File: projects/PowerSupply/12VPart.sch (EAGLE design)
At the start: 26 parts, among them IC1 LM2596T, IC2 LM2596T, X1 IN, X2 OUT

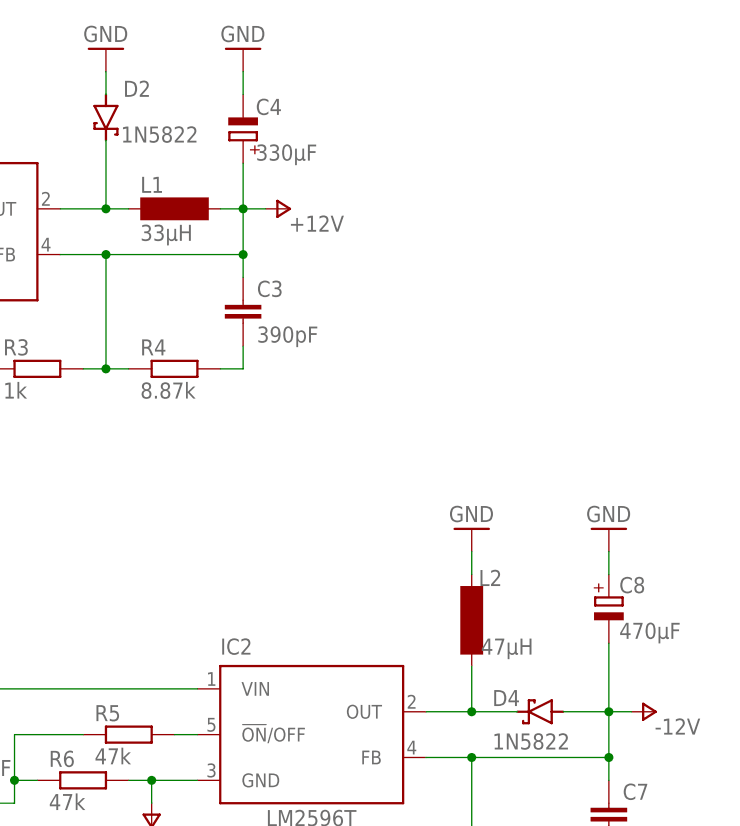
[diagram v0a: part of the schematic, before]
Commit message: feat: 12 volt part modified
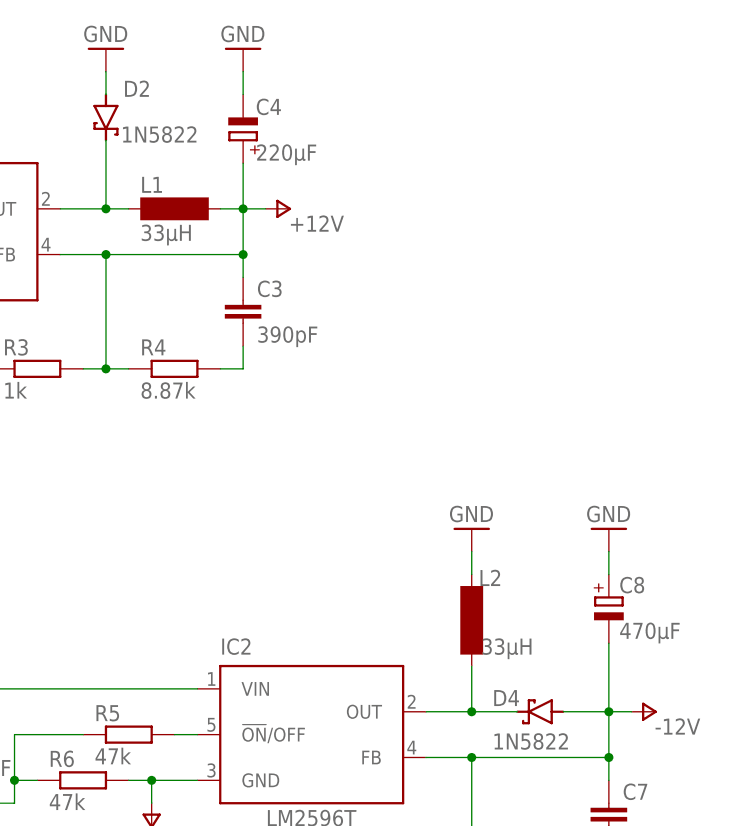
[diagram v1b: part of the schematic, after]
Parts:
- C4: value 330µF -> 220µF
- L1: device inductor-neosid:SD12-680 -> bb84:IND-120-330K
- L2: value 47µH -> 33µH; device inductor-neosid:SD12-680 -> bb84:IND-120-330K
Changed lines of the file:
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@@
 <grid distance="0.1" unitdist="inch" unit="inch" style="lines" multiple="1" display="no" altdistance="0.01" altunitdist="inch" altunit="inch"/>
 <layers>
-<layer number="1" name="Top" color="4" fill="1" visible="no" active="no"/>
-<layer number="16" name="Bottom" color="1" fill="1" visible="no" active="no"/>
-<layer number="17" name="Pads" color="2" fill="1" visible="no" active="no"/>
-<layer number="18" name="Vias" color="2" fill="1" visible="no" active="no"/>
-<layer number="19" name="Unrouted" color="6" fill="1" visible="no" active="no"/>
-<layer number="20" name="Dimension" color="24" fill="1" visible="no" active="no"/>
-<layer number="21" name="tPlace" color="7" fill="1" visible="no" active="no"/>
-<layer number="22" name="bPlace" color="7" fill="1" visible="no" active="no"/>
-<layer number="23" name="tOrigins" color="15" fill="1" visible="no" active="no"/>
-<layer number="24" name="bOrigins" color="15" fill="1" visible="no" active="no"/>
-<layer number="25" name="tNames" color="7" fill="1" visible="no" active="no"/>
-<layer number="26" name="bNames" color="7" fill="1" visible="no" active="no"/>
-<layer number="27" name="tValues" color="7" fill="1" visible="no" active="no"/>
-<layer number="28" name="bValues" color="7" fill="1" visible="no" active="no"/>
+<layer number="1" name="Top" color="4" fill="1" visible="yes" active="no"/>
+<layer number="16" name="Bottom" color="1" fill="1" visible="yes" active="no"/>
+<layer number="17" name="Pads" color="2" fill="1" visible="yes" active="no"/>
+<layer number="18" name="Vias" color="2" fill="1" visible="yes" active="no"/>
+<layer number="19" name="Unrouted" color="6" fill="1" visible="yes" active="no"/>
+<layer number="20" name="Dimension" color="24" fill="1" visible="yes" active="no"/>
+<layer number="21" name="tPlace" color="7" fill="1" visible="yes" active="no"/>
+<layer number="22" name="bPlace" color="7" fill="1" visible="yes" active="no"/>
+<layer number="23" name="tOrigins" color="15" fill="1" visible="yes" active="no"/>
+<layer number="24" name="bOrigins" color="15" fill="1" visible="yes" active="no"/>
+<layer number="25" name="tNames" color="7" fill="1" visible="yes" active="no"/>
+<layer number="26" name="bNames" color="7" fill="1" visible="yes" active="no"/>
+<layer number="27" name="tValues" color="7" fill="1" visible="yes" active="no"/>
+<layer number="28" name="bValues" color="7" fill="1" visible="yes" active="no"/>
 <layer number="29" name="tStop" color="7" fill="3" visible="no" active="no"/>
 <layer number="30" name="bStop" color="7" fill="6" visible="no" active="no"/>
@@
 <layer number="35" name="tGlue" color="7" fill="4" visible="no" active="no"/>
 <layer number="36" name="bGlue" color="7" fill="5" visible="no" active="no"/>
-<layer number="37" name="tTest" color="7" fill="1" visible="no" active="no"/>
-<layer number="38" name="bTest" color="7" fill="1" visible="no" active="no"/>
+<layer number="37" name="tTest" color="7" fill="1" visible="yes" active="no"/>
+<layer number="38" name="bTest" color="7" fill="1" visible="yes" active="no"/>
 <layer number="39" name="tKeepout" color="4" fill="11" visible="no" active="no"/>
 <layer number="40" name="bKeepout" color="1" fill="11" visible="no" active="no"/>
@@
 <layer number="44" name="Drills" color="7" fill="1" visible="no" active="no"/>
 <layer number="45" name="Holes" color="7" fill="1" visible="no" active="no"/>
-<layer number="46" name="Milling" color="3" fill="1" visible="no" active="no"/>
-<layer number="47" name="Measures" color="7" fill="1" visible="no" active="no"/>
-<layer number="48" name="Document" color="7" fill="1" visible="no" active="no"/>
-<layer number="49" name="Reference" color="7" fill="1" visible="no" active="no"/>
-<layer number="51" name="tDocu" color="7" fill="1" visible="no" active="no"/>
-<layer number="52" name="bDocu" color="7" fill="1" visible="no" active="no"/>
+<layer number="46" name="Milling" color="3" fill="1" visible="yes" active="no"/>
+<layer number="47" name="Measures" color="7" fill="1" visible="yes" active="no"/>
+<layer number="48" name="Document" color="7" fill="1" visible="yes" active="no"/>
+<layer number="49" name="Reference" color="7" fill="1" visible="yes" active="no"/>
+<layer number="51" name="tDocu" color="7" fill="1" visible="yes" active="no"/>
+<layer number="52" name="bDocu" color="7" fill="1" visible="yes" active="no"/>
 <layer number="88" name="SimResults" color="9" fill="1" visible="yes" active="yes"/>
 <layer number="89" name="SimProbes" color="9" fill="1" visible="yes" active="yes"/>
@@
 <part name="D2" library="diode" library_urn="urn:adsk.eagle:library:210" deviceset="SCHOTTKY-DIODE" device="C4111-15" package3d_urn="urn:adsk.eagle:package:43355/2" value="1N5822"/>
 <part name="GND5" library="supply1" library_urn="urn:adsk.eagle:library:371" deviceset="GND" device=""/>
-<part name="L1" library="inductor-neosid" library_urn="urn:adsk.eagle:library:241" deviceset="SD12" device="-680" package3d_urn="urn:adsk.eagle:package:14657/1" value="33µH"/>
-<part name="C4" library="rcl" library_urn="urn:adsk.eagle:library:334" deviceset="CPOL-EU" device="E3.5-8" package3d_urn="urn:adsk.eagle:package:23360/2" value="330µF"/>
+<part name="L1" library="bb84" deviceset="IND-120-330K" device="" value="33µH"/>
+<part name="C4" library="rcl" library_urn="urn:adsk.eagle:library:334" deviceset="CPOL-EU" device="E3.5-8" package3d_urn="urn:adsk.eagle:package:23360/2" value="220µF"/>
 <part name="X2" library="con-wago-508" library_urn="urn:adsk.eagle:library:196" deviceset="W237-03P" device="" package3d_urn="urn:adsk.eagle:package:10737/1" value="OUT"/>
 <part name="GND7" library="supply1" library_urn="urn:adsk.eagle:library:371" deviceset="GND" device=""/>
 <part name="IC2" library="national-semiconductor" library_urn="urn:adsk.eagle:library:307" deviceset="LM2596" device="T" package3d_urn="urn:adsk.eagle:package:21216/1"/>
-<part name="L2" library="inductor-neosid" library_urn="urn:adsk.eagle:library:241" deviceset="SD12" device="-680" package3d_urn="urn:adsk.eagle:package:14657/1" value="47µH"/>
+<part name="L2" library="bb84" deviceset="IND-120-330K" device="" value="33µH"/>
 <part name="GND9" library="supply1" library_urn="urn:adsk.eagle:library:371" deviceset="GND" device=""/>
 <part name="D4" library="diode" library_urn="urn:adsk.eagle:library:210" deviceset="SCHOTTKY-DIODE" device="C4111-15" package3d_urn="urn:adsk.eagle:package:43355/2" value="1N5822"/>

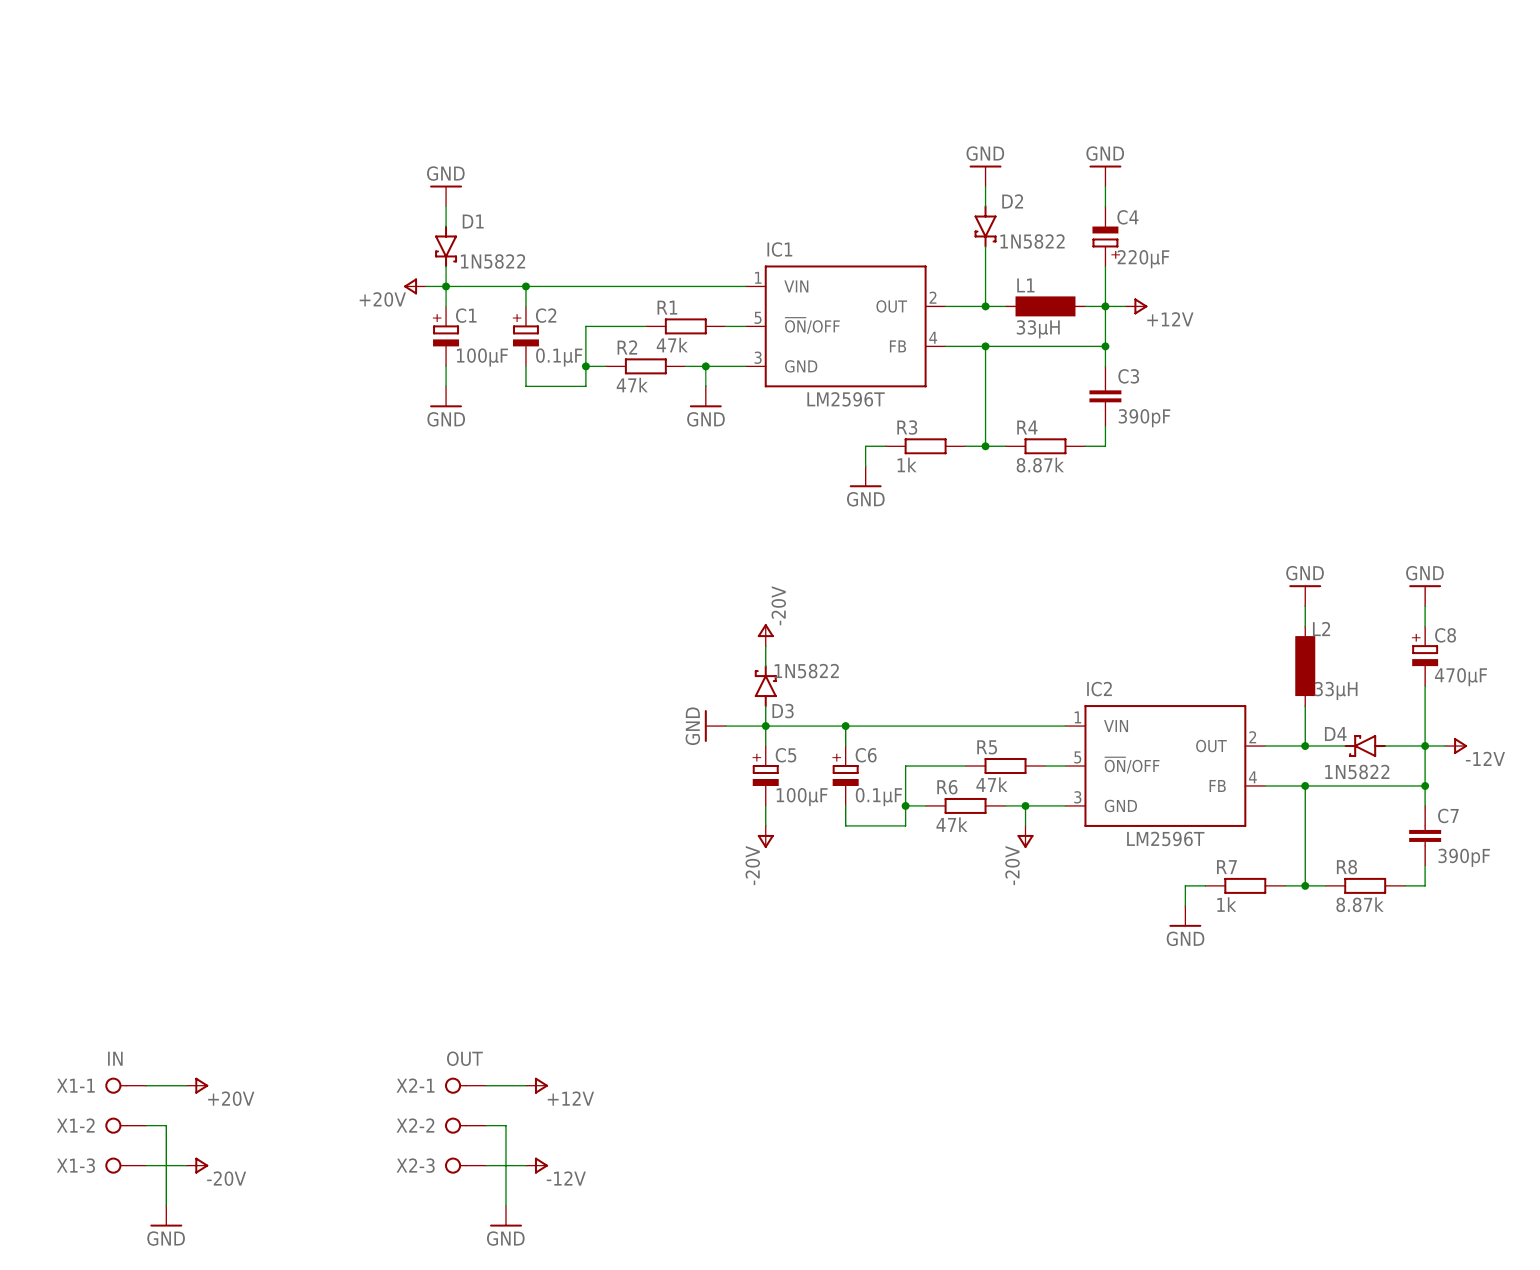
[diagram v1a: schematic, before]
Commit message: feat: modified 12 volt parts
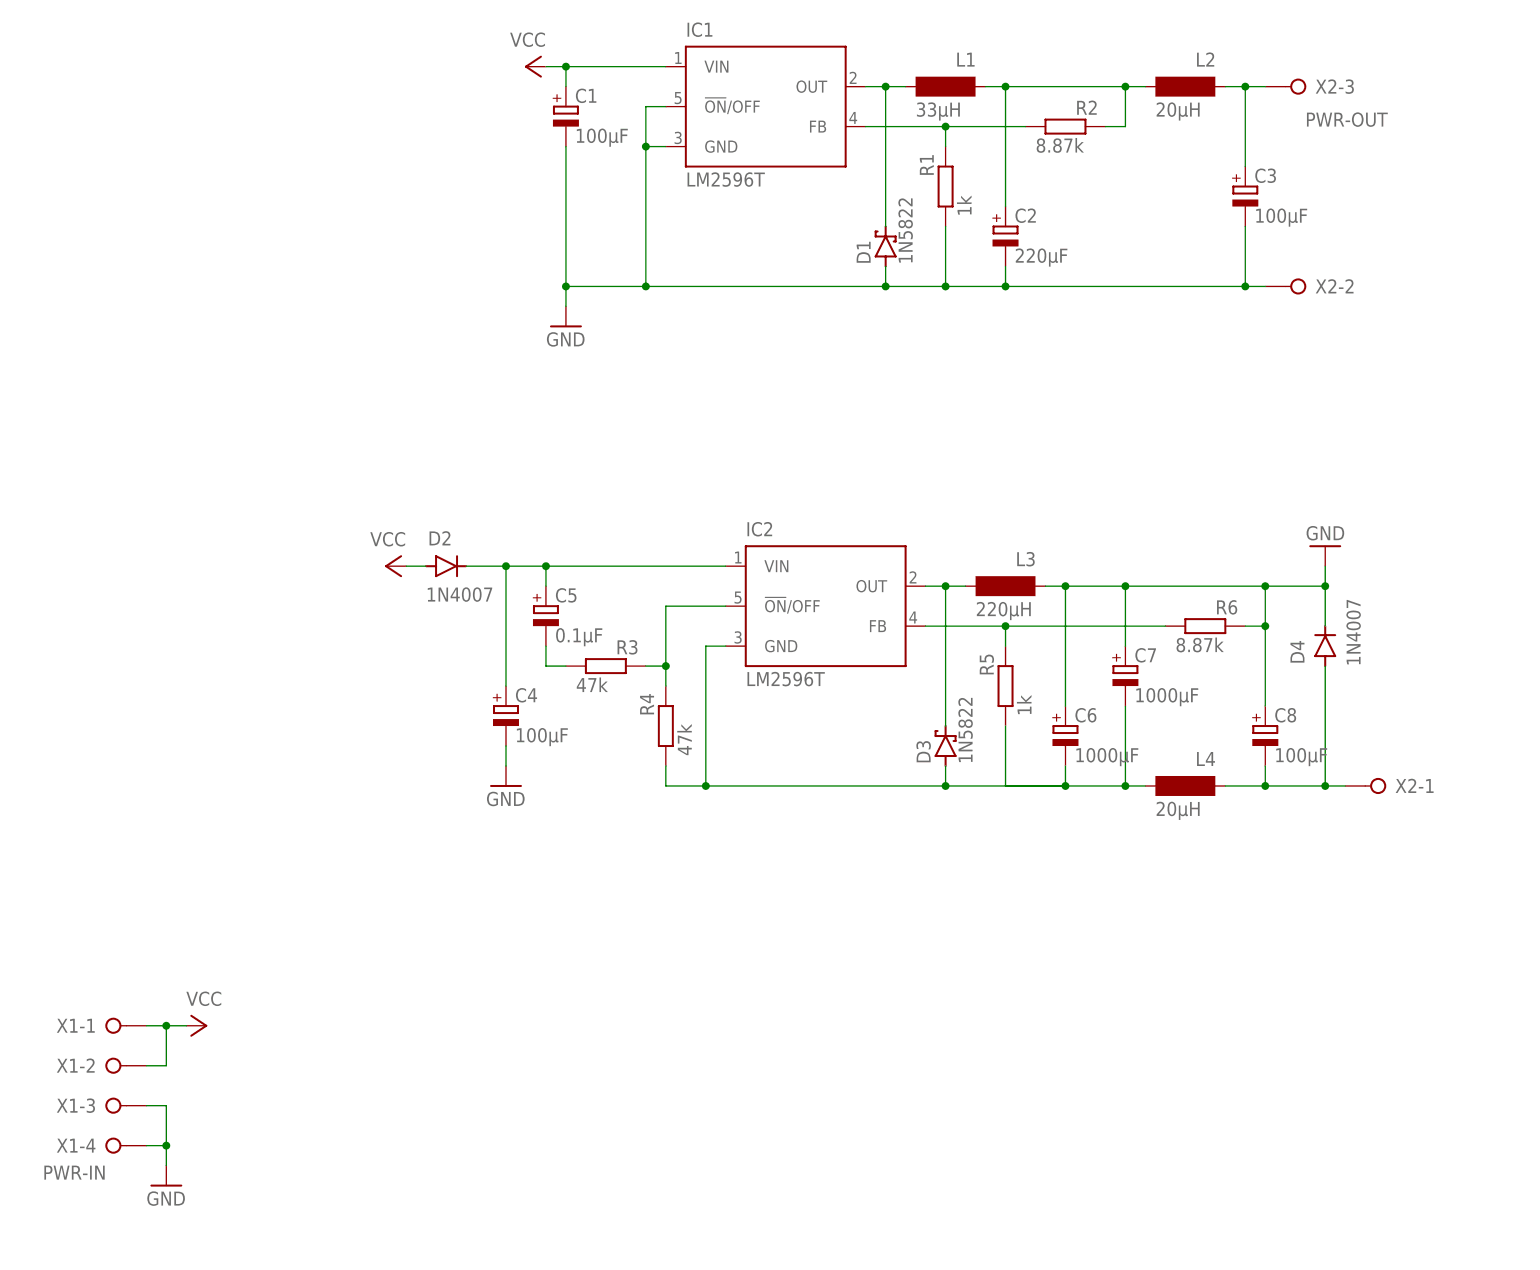
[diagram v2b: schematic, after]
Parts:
- removed R7: 1k, rcl:R-EU_0207/10
- removed R8: 8.87k, rcl:R-EU_0207/10
- added L3: 220µH, bb84:11PHC-221K-50
- added L4: 20µH, bb84:B82111B0000C020
- C2: value 0.1µF -> 220µF; device rcl:CPOL-EUE1.8-4 -> rcl:CPOL-EUE2.5-6
- C3: value 390pF -> 100µF; device rcl:C-EU050-024X044 -> rcl:CPOL-EUE2.5-6
- C4: value 220µF -> 100µF; device rcl:CPOL-EUE3.5-8 -> rcl:CPOL-EUE2.5-6
- C5: value 100µF -> 0.1µF; device rcl:CPOL-EUE2.5-6 -> rcl:CPOL-EUE2-4
- C6: value 0.1µF -> 1000µF; device rcl:CPOL-EUE1.8-4 -> rcl:CPOL-EUE5-10.5
- C7: value 390pF -> 1000µF; device rcl:C-EU050-024X044 -> rcl:CPOL-EUE5-10.5
- C8: value 470µF -> 100µF; device rcl:CPOL-EUE3.5-8 -> rcl:CPOL-EUE2.5-6
- D1, D3: device diode:SCHOTTKY-DIODEC4111-15 -> diode:1N5908
- D2, D4: value 1N5822 -> 1N4007; device diode:SCHOTTKY-DIODEC4111-15 -> Diodes:1N4007
- L2: value 33µH -> 20µH; device bb84:IND-120-330K -> bb84:B82111B0000C020
- R1, R5: value 47k -> 1k
- R2, R6: value 47k -> 8.87k
- R3: value 1k -> 47k
- R4: value 8.87k -> 47k
- X1: value IN -> PWR-IN; device con-wago-508:W237-03P -> con-wago-508:W237-04P
- X2: value OUT -> PWR-OUT
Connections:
- removed net +12V: C3.1, C4.+, IC1.FB, L1.2, R3.2, R4.1, X2-1.KL
- removed net +20V: C1.+, C2.+, D1.C, IC1.VIN, X1-1.KL
- removed net -12V: C7.1, C8.-, D4.A, IC2.FB, R7.2, R8.1, X2-3.KL
- removed net -20V: C5.-, D3.C, IC2.GND, R6.2, X1-3.KL
- removed net N$2: D4.C, IC2.OUT, L2.1
- removed net N$8: C6.-, R5.1, R6.1
- new net N$10: IC2.!ON!/OFF, R3.2, R4.2
- new net N$11: C6.-, C7.-, D3.A, IC2.GND, L4.1, R4.1, R5.1
- new net N$12: D3.C, IC2.OUT, L3.1
- new net N$14: IC2.FB, R5.2, R6.1
- new net N$9: C5.-, R3.1
- new net VCC: C1.+, D2.A, IC1.VIN, X1-1.KL, X1-2.KL
- net GND: now also C2.-, C3.-, C7.+, D4.C, IC1.!ON!/OFF, L3.2, R1.1, R6.2, X1-3.KL, X1-4.KL; no longer C5.+, D2.A, D3.A, IC2.VIN, L2.2, R2.2, R3.1, R7.1, X1-2.KL
- net N$1: now also C4.+, C5.+, D2.C, IC2.VIN; no longer C3.2, R4.2
- net N$3: now also C8.-, D4.A, L4.2, X2-1.KL; no longer D2.C, IC1.OUT, L1.1
- net N$4: now also D1.C, IC1.OUT, L1.1; no longer IC1.!ON!/OFF, R1.2
- net N$5: now also IC1.FB, R1.2, R2.1; no longer C7.2, R8.2
- net N$6: now also C2.+, L1.2, L2.1, R2.2; no longer C2.-, R1.1, R2.1
- net N$7: now also C3.+, L2.2, X2-3.KL; no longer IC2.!ON!/OFF, R5.2
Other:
- moved on the sheet: C1, C2, C4, C5, C6, C8, IC1, IC2, L1, L2, R1, R2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
